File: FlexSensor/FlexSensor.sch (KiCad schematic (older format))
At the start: 159 parts

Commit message: Added USB connection
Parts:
- removed C?: 100nF, symbol Device:C_Small
- removed D? (x2): 1N5821, Diode_THT:D_DO-201AD_P15.24mm_Horizontal, symbol Diode:1N5821
- removed U?: 74HC165, symbol Trainiot:74HC165
- removed U?: 74HC590, symbol 74xx:74HC590
- removed U?: 74HC595, symbol Trainiot:74HC595
- added C? (x3): 100nF, symbol Device:C_Small
- added C?: 4.7μF, symbol Device:CP
- added C?: 1μF, symbol Device:C_Small
- added D?: 1N4007, symbol Device:D
- added J?: USB_B_Micro, symbol Connector:USB_B_Micro
- added R?: 470, symbol Device:R
- added R?: 10K, symbol Device:R
- added U? (x2): 74HC595, symbol 74xx:74HC595
- added U?: CP2102, symbol Trainiot:CP2102
- added U?: 74HC165, symbol 74xx:74LS165
- D?: value 1N5821 -> 1N5819
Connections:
- net BTN_AND_REVISION is gone; now on net MISO_AND_REVISION: U?.5 (SENS_VN)
- net +3V3: now also C?.1, C?.1, C?.1, C?.1, C?.1, R?.2, U?.10 (~SRCLR), U?.10 (~SRCLR), U?.16 (VCC), U?.16 (VCC), U?.16 (VCC), U?.6 (VDD), U?.7 (REGIN)
- net ADR0_VDD: now also R?.2, U?.16 (O1)
- net ADR1_VDD: now also R?.2, U?.15 (O2)
- net ADR2_VDD: now also R?.2, U?.14 (O3)
- net ADR3_VDD: now also R?.2, U?.13 (O4)
- net ADR4_VDD: now also R?.2, U?.12 (O5)
- net ADR5_VDD: now also R?.2, U?.11 (O6)
- net BOOTING: now also U?.13 (~OE), U?.13 (~OE)
- net BUTTON: now also R?.1, U?.11 (D0)
- net GND: now also C?.2, C?.2, C?.2, C?.2, C?.2, J?.5 (GND), J?.6 (Shield), U?.3 (GND), U?.4 (D5), U?.5 (D6), U?.6 (D7), U?.8 (GND), U?.8 (GND), U?.8 (GND)
- net LED_B: now also U?.3 (QD)
- net LED_G: now also U?.2 (QC)
- net LED_R: now also U?.1 (QB)
- net MISO_AND_REVISION: no longer R?.1
- net PULL_DOWN: now also U?.7 (QH)
- net SPI_CLK: now also U?.11 (SRCLK), U?.11 (SRCLK), U?.2 (CP)
- net SPI_MOSI: now also U?.14 (SER)
- net SPI_MOSI_2: now also U?.9 (QH')
- net SPI_SS: now also U?.1 (~PL)
- net UART_CTS: now also U?.6 (IO34); no longer U?.7 (IO35)
- net UART_RTS: now also U?.9 (IO33); no longer U?.8 (IO32)
- net UART_RX: now also U?.7 (IO35); no longer U?.6 (IO34), U?.9 (IO33)
- net USB5V: now also D?.2 (A), J?.1 (VBUS), U?.8 (VBUS)
- net ~S88_IN_CLK: now also U?.13 (D2)
- net ~S88_IN_DATA: now also U?.6 (QG)
- net ~S88_IN_LOAD: now also U?.12 (D1)
- net ~S88_OUT_CLK: now also U?.5 (QF)
- net ~S88_OUT_DATA: now also U?.14 (D3)
- net ~S88_OUT_LOAD: now also U?.7 (QH)
- net ~S88_OUT_RESET: now also U?.4 (QE)
- net ~S88_TRACK: now also U?.3 (D4)
- net ~SPI_SS: now also U?.12 (RCLK), U?.12 (RCLK), U?.15 (~CE)
- net S88_IN_DATA: now reaches J?.1 (Pin_1), J?.2, Q?.2 (E), Q?.2 (E)
- net S88_IN_CLOCK: now reaches J?.3 (Pin_3), J?.4, R?.1, U?.5 (+)
- net S88_IN_LOAD: now reaches J?.4 (Pin_4), J?.6, R?.1, U?.5 (+)
- net S88_IN_RESET: now reaches J?.5 (Pin_5), J?.7
- net S88_IN_VCC: now reaches J?.1, J?.6 (Pin_6), Q?.3 (C)
- net at C?.1, C?.1, C?.1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: now also D?.1 (K)
- net at U?.11 (S1): now also U?.9 (Q7)
- net at R?.2, U?.13 (1Y1): now also R?.1
- net ADR5: now reaches U?.1 (I1)
- net ADR5: now also U?.5 (QF)
- net ADR4: now reaches U?.2 (I2)
- net ADR4: now also U?.4 (QE)
- net ADR3: now reaches U?.3 (I3)
- net ADR3: now also U?.3 (QD)
- net ADR2: now reaches U?.4 (I4)
- net ADR2: now also U?.2 (QC)
- net ADR1: now reaches U?.5 (I5)
- net ADR1: now also U?.1 (QB)
- net ADR0: now reaches U?.6 (I6)
- net ADR0: now also U?.15 (QA)
- net DTR renamed ~DTR
- net ~DTR: now also U?.28 (~DTR)
- net RTS renamed ~RTS
- net ~RTS: now also U?.24 (~RTS)
- net RXD0 renamed USB_RXD
- net USB_RXD: now also U?.25 (RXD)
- net TXD0 renamed USB_TXD
- net USB_TXD: now also R?.1
- net XPRESSNET_ENABLE renamed XPRESSNET_TX_ENABLE
- new net: U?.14 (SER), U?.9 (QH')
- new net: R?.2, U?.26 (TXD)
- new net: J?.3 (D+), U?.4 (D+)
- new net: J?.2 (D-), U?.5 (D-)
- new net UART_TX: U?.8 (IO32)
- no-connect marks 16 -> 24
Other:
- note added: "Pull down strength\ndetermine board\nrevision."
- note added: "Too big voltage drop for 3.3V regulator?\nWant to favor external 5V over USB 5V - maybe with a mosfet closed when external power is available."
- note added: "USB"
- note removed: "Figure out mosfet construction?\nIdeal external should "win" if 3V+"
- note removed: "Inrush limit needed?"
- note removed: "Move to pin out, add address bits in second shift register?"
- moved on the sheet: C?, D?, R?, U?, U?A

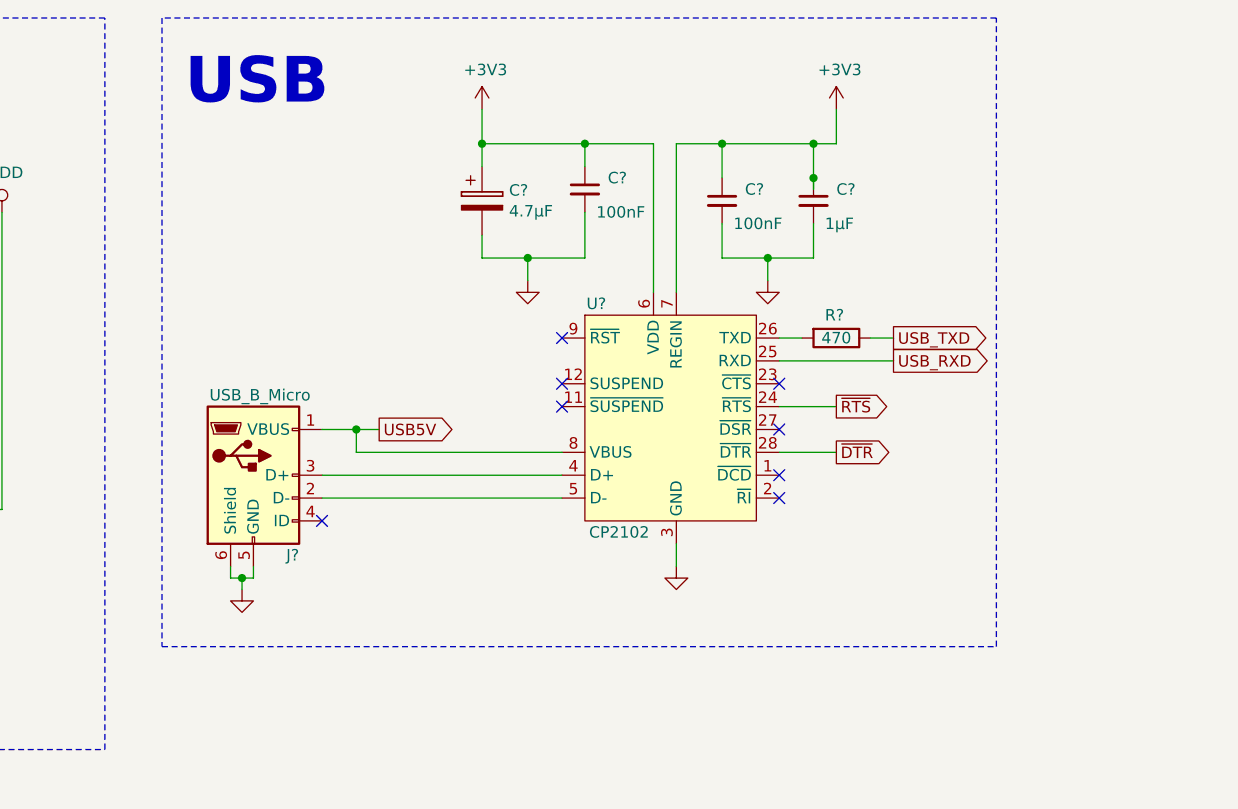
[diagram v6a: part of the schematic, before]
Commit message: Added UART header to allow programming without adding USB support (cheaper, less soldering)
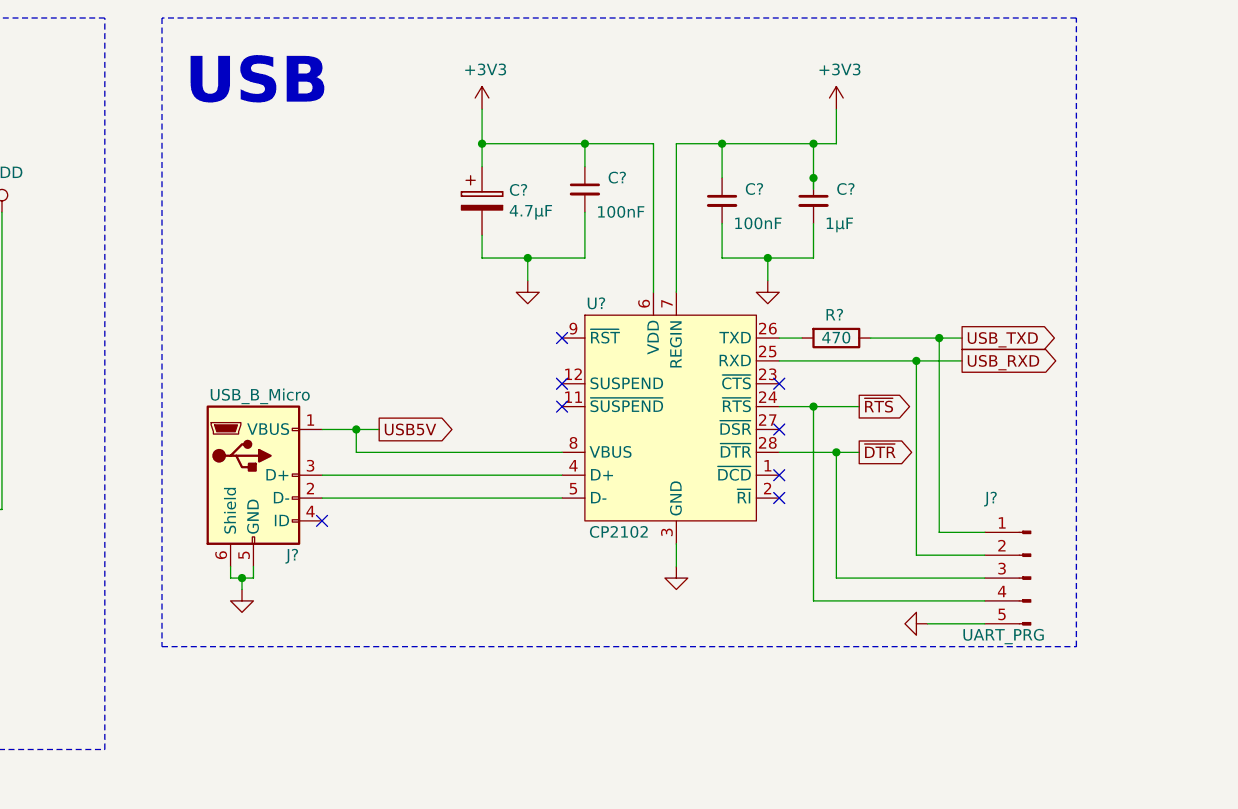
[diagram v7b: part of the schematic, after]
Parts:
- added J?: UART_PRG, symbol Connector:Conn_01x05_Male
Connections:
- net GND: now also J?.5 (Pin_5)
- net USB_RXD: now also J?.2 (Pin_2)
- net USB_TXD: now also J?.1 (Pin_1)
- net ~DTR: now also J?.3 (Pin_3)
- net ~RTS: now also J?.4 (Pin_4)
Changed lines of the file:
@@
 Wire Wire Line
 	15850 2750 16100 2750
-Text GLabel 16100 2750 2    50   Output ~ 0
+Text GLabel 16200 2750 2    50   Output ~ 0
 ~DTR
 Wire Wire Line
-	15850 2550 16100 2550
-Text GLabel 16100 2550 2    50   Output ~ 0
+	15850 2550 16000 2550
+Text GLabel 16200 2550 2    50   Output ~ 0
 ~RTS
 Wire Wire Line
-	15850 2350 16350 2350
-Text GLabel 16350 2350 2    50   Output ~ 0
+	15850 2350 16450 2350
+Text GLabel 16650 2350 2    50   Output ~ 0
 USB_RXD
 $Comp
@@
 	15950 2250 15850 2250
 Wire Wire Line
-	16250 2250 16350 2250
-Text GLabel 16350 2250 2    50   Output ~ 0
+	16250 2250 16550 2250
+Text GLabel 16650 2250 2    50   Output ~ 0
 USB_TXD
 NoConn ~ 15850 2450
@@
 	13150 850  13150 3600
 Wire Notes Line
-	13150 3600 16800 3600
-Wire Notes Line
-	16800 3600 16800 850
-Wire Notes Line
-	16800 850  13150 850
+	13150 3600 17150 3600
+Wire Notes Line
+	17150 3600 17150 850
+Wire Notes Line
+	17150 850  13150 850
 Text Notes 13250 1250 0    200  ~ 40
 USB
@@
 Text Notes 2950 1400 0    50   ~ 0
 Too big voltage drop for 3.3V regulator?\nWant to favor external 5V over USB 5V - maybe with a mosfet closed when external power is available.
+$Comp
+L Connector:Conn_01x05_Male J?
+U 1 1 5D730C02
+P 16950 3300
+F 0 "J?" H 17150 3650 50  0000 R CNN
+F 1 "UART_PRG" H 17250 3050 50  0000 R CNN
+F 2 "" H 16950 3300 50  0001 C CNN
+F 3 "~" H 16950 3300 50  0001 C CNN
+	1    16950 3300
+	-1   0    0    -1
+$EndComp
+Wire Wire Line
+	16750 3100 16550 3100
+Wire Wire Line
+	16550 3100 16550 2250
+Connection ~ 16550 2250
+Wire Wire Line
+	16550 2250 16650 2250
+Wire Wire Line
+	16450 2350 16450 3200
+Wire Wire Line
+	16450 3200 16750 3200
+Connection ~ 16450 2350
+Wire Wire Line
+	16450 2350 16650 2350
+Wire Wire Line
+	16100 2750 16100 3300
+Wire Wire Line
+	16100 3300 16750 3300
+Connection ~ 16100 2750
+Wire Wire Line
+	16100 2750 16200 2750
+Wire Wire Line
+	16000 2550 16000 3400
+Wire Wire Line
+	16000 3400 16750 3400
+Connection ~ 16000 2550
+Wire Wire Line
+	16000 2550 16200 2550
+Wire Wire Line
+	16750 3500 16500 3500
 Wire Bus Line
 	3350 14400 4950 14400
@@
 Wire Bus Line
 	4950 5150 4950 14400
+$Comp
+L power:GND #PWR?
+U 1 1 5E1D0744
+P 16500 3500
+F 0 "#PWR?" H 16500 3250 50  0001 C CNN
+F 1 "GND" H 16650 3450 50  0001 C TNN
+F 2 "" H 16500 3500 50  0001 C CNN
+F 3 "" H 16500 3500 50  0001 C CNN
+	1    16500 3500
+	0    1    1    0
+$EndComp
 $EndSCHEMATC

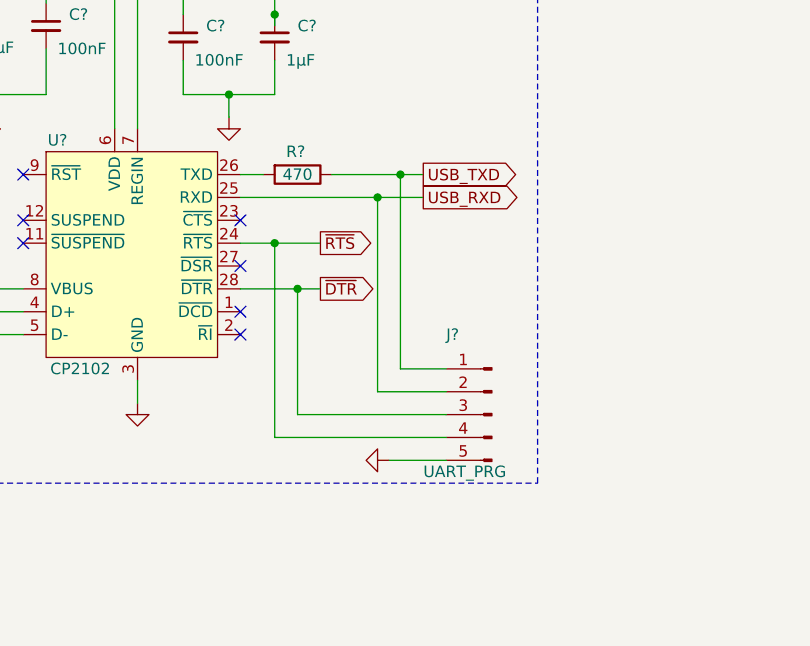
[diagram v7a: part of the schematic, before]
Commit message: Added 5V pin to the UART programming interface to allow powering from an USB adapter easily.
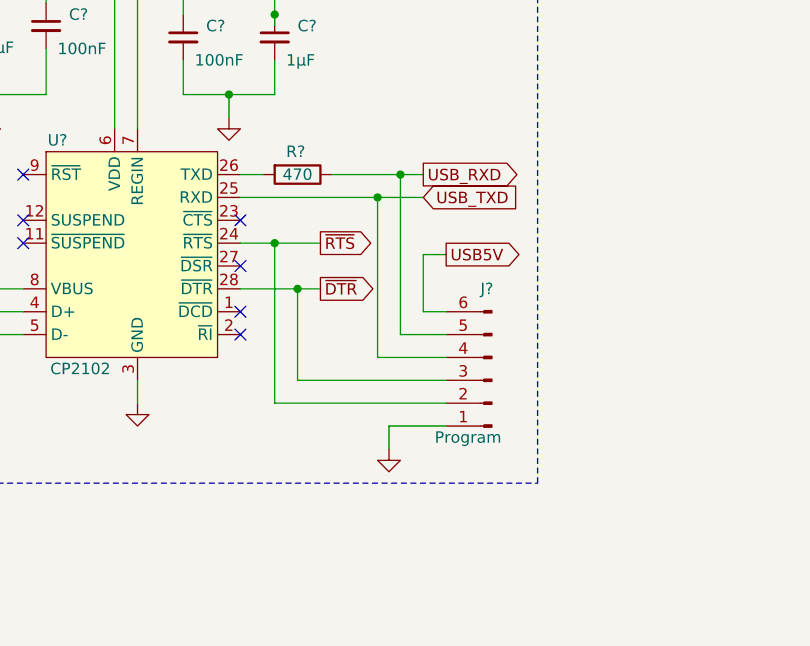
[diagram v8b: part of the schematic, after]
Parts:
- removed J?: UART_PRG, symbol Connector:Conn_01x05_Male
- added J?: Program, symbol Connector:Conn_01x06_Male
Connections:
- net GND: now also J?.1 (Pin_1)
- net USB5V: now also J?.6 (Pin_6)
- net USB_RXD: now also R?.1, J?.5 (Pin_5); no longer U?.25 (RXD)
- net USB_TXD: now also U?.25 (RXD), J?.4 (Pin_4); no longer R?.1
- net ~DTR: now also J?.3 (Pin_3)
- net ~RTS: now also J?.2 (Pin_2)
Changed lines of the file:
@@
 Wire Wire Line
 	15850 2350 16450 2350
-Text GLabel 16650 2350 2    50   Output ~ 0
+Text GLabel 16650 2250 2    50   Output ~ 0
 USB_RXD
 $Comp
@@
 Wire Wire Line
 	16250 2250 16550 2250
-Text GLabel 16650 2250 2    50   Output ~ 0
+Text GLabel 16650 2350 2    50   Input ~ 0
 USB_TXD
 NoConn ~ 15850 2450
@@
 Text Notes 2950 1400 0    50   ~ 0
 Too big voltage drop for 3.3V regulator?\nWant to favor external 5V over USB 5V - maybe with a mosfet closed when external power is available.
-$Comp
-L Connector:Conn_01x05_Male J?
-U 1 1 5D730C02
-P 16950 3300
-F 0 "J?" H 17150 3650 50  0000 R CNN
-F 1 "UART_PRG" H 17250 3050 50  0000 R CNN
-F 2 "" H 16950 3300 50  0001 C CNN
-F 3 "~" H 16950 3300 50  0001 C CNN
-	1    16950 3300
-	-1   0    0    -1
-$EndComp
-Wire Wire Line
-	16750 3100 16550 3100
-Wire Wire Line
-	16550 3100 16550 2250
+Wire Wire Line
+	16750 2950 16550 2950
+Wire Wire Line
+	16550 2950 16550 2250
 Connection ~ 16550 2250
 Wire Wire Line
 	16550 2250 16650 2250
 Wire Wire Line
-	16450 2350 16450 3200
-Wire Wire Line
-	16450 3200 16750 3200
+	16450 2350 16450 3050
+Wire Wire Line
+	16450 3050 16750 3050
 Connection ~ 16450 2350
 Wire Wire Line
 	16450 2350 16650 2350
 Wire Wire Line
-	16100 2750 16100 3300
-Wire Wire Line
-	16100 3300 16750 3300
+	16100 2750 16100 3150
+Wire Wire Line
+	16100 3150 16750 3150
 Connection ~ 16100 2750
 Wire Wire Line
 	16100 2750 16200 2750
 Wire Wire Line
-	16000 2550 16000 3400
-Wire Wire Line
-	16000 3400 16750 3400
+	16000 2550 16000 3250
+Wire Wire Line
+	16000 3250 16750 3250
 Connection ~ 16000 2550
 Wire Wire Line
 	16000 2550 16200 2550
 Wire Wire Line
-	16750 3500 16500 3500
+	16750 3350 16500 3350
+$Comp
+L power:GND #PWR?
+U 1 1 5E1D0744
+P 16500 3450
+F 0 "#PWR?" H 16500 3200 50  0001 C CNN
+F 1 "GND" H 16650 3400 50  0001 C TNN
+F 2 "" H 16500 3450 50  0001 C CNN
+F 3 "" H 16500 3450 50  0001 C CNN
+	1    16500 3450
+	1    0    0    -1
+$EndComp
+Wire Wire Line
+	16500 3450 16500 3350
+$Comp
+L Connector:Conn_01x06_Male J?
+U 1 1 5B0BC9AF
+P 16950 3150
+F 0 "J?" H 17000 2750 50  0000 R CNN
+F 1 "Program" H 17200 3400 50  0000 R CNN
+F 2 "" H 16950 3150 50  0001 C CNN
+F 3 "~" H 16950 3150 50  0001 C CNN
+	1    16950 3150
+	-1   0    0    1
+$EndComp
+Text GLabel 16750 2600 2    50   Output ~ 0
+USB5V
+Wire Wire Line
+	16750 2850 16650 2850
+Wire Wire Line
+	16650 2850 16650 2600
+Wire Wire Line
+	16650 2600 16750 2600
 Wire Bus Line
 	3350 14400 4950 14400
@@
 Wire Bus Line
 	4950 5150 4950 14400
-$Comp
-L power:GND #PWR?
-U 1 1 5E1D0744
-P 16500 3500
-F 0 "#PWR?" H 16500 3250 50  0001 C CNN
-F 1 "GND" H 16650 3450 50  0001 C TNN
-F 2 "" H 16500 3500 50  0001 C CNN
-F 3 "" H 16500 3500 50  0001 C CNN
-	1    16500 3500
-	0    1    1    0
-$EndComp
 $EndSCHEMATC
